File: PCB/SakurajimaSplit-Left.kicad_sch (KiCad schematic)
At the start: 31 parts, among them J1 SWD, J2 USB-C to Right-Half, J3 VREF+, SW1 SWCLK/BOOT0, U1 USBLC6-2SC6, U10 ZJY_M233, U2 STM32G0B1CBT6, U3 W25Q128JVS, Y1 8MHz

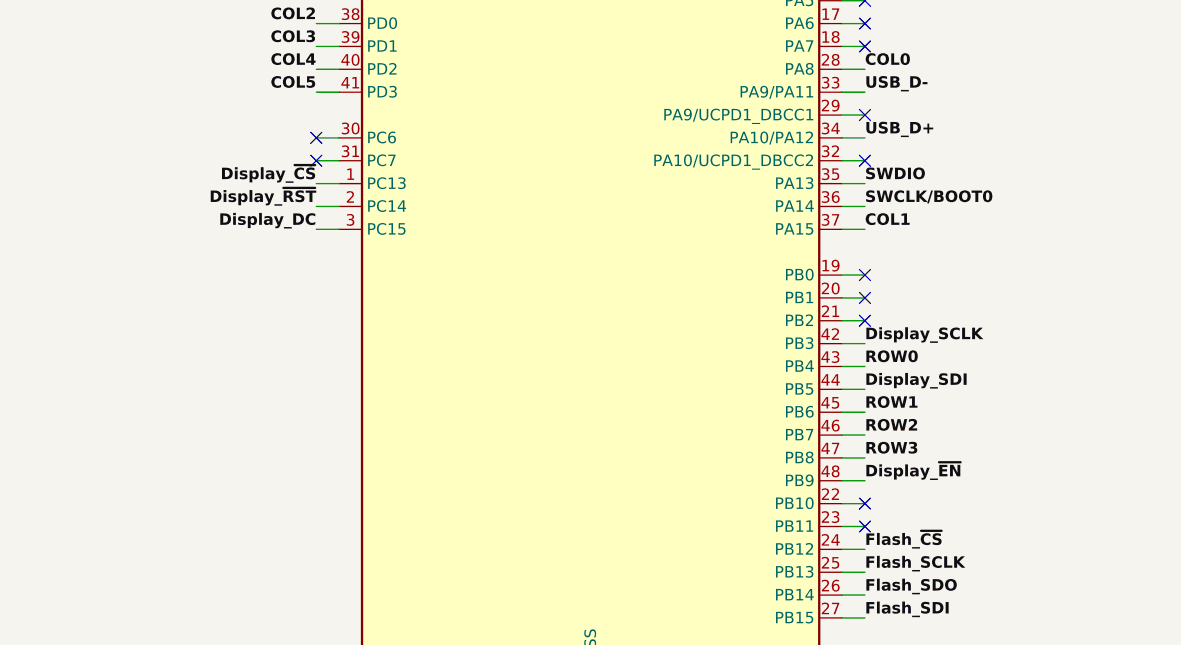
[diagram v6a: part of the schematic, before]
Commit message: feat(pcb): route left half
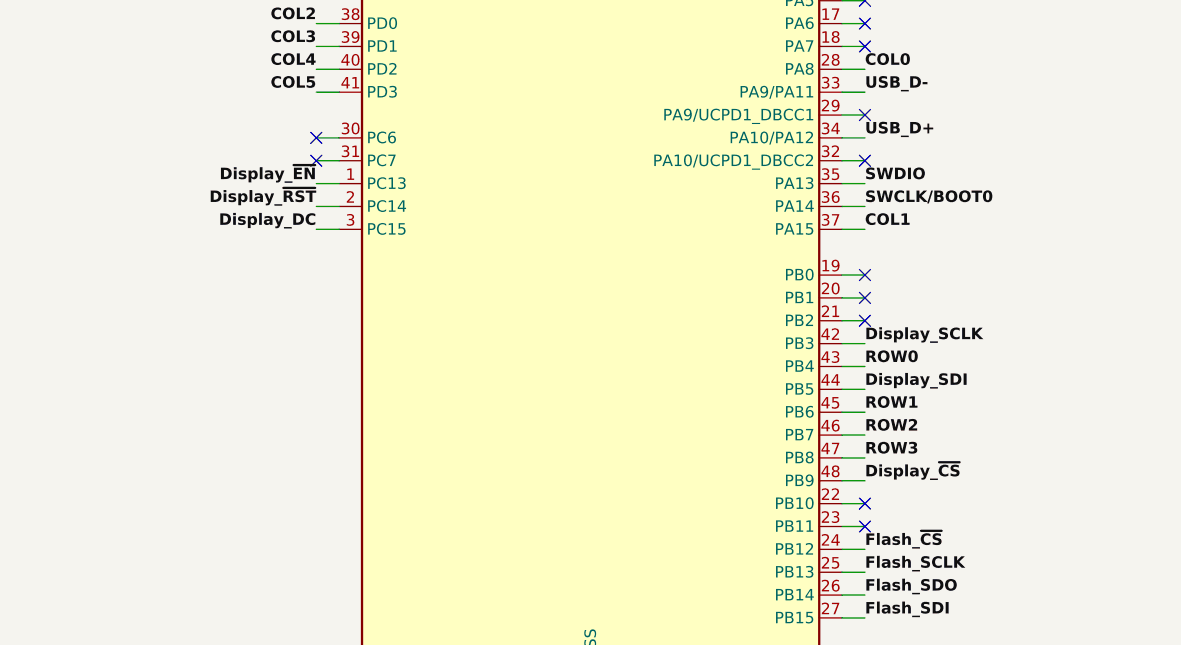
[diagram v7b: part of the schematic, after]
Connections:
- net Display_~{CS}: now also U2.48 (PB9); no longer U2.1 (PC13)
- net Display_~{EN}: now also U2.1 (PC13); no longer U2.48 (PB9)
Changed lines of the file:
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@@
 	)
 	(label "Display_~{CS}"
-		(at 179.07 147.32 180)
-		(effects
-			(font
-				(size 1.27 1.27)
-				(thickness 0.254)
-				(bold yes)
-			)
-			(justify right bottom)
+		(at 240.03 180.34 0)
+		(effects
+			(font
+				(size 1.27 1.27)
+				(thickness 0.254)
+				(bold yes)
+			)
+			(justify left bottom)
 		)
 	)
@@
 	)
 	(label "Display_~{EN}"
-		(at 240.03 180.34 0)
-		(effects
-			(font
-				(size 1.27 1.27)
-				(thickness 0.254)
-				(bold yes)
-			)
-			(justify left bottom)
-		)
-	)
+		(at 179.07 147.32 180)
+		(effects
+			(font
+				(size 1.27 1.27)
+				(thickness 0.254)
+				(bold yes)
+			)
+			(justify right bottom)
+		)
+	)

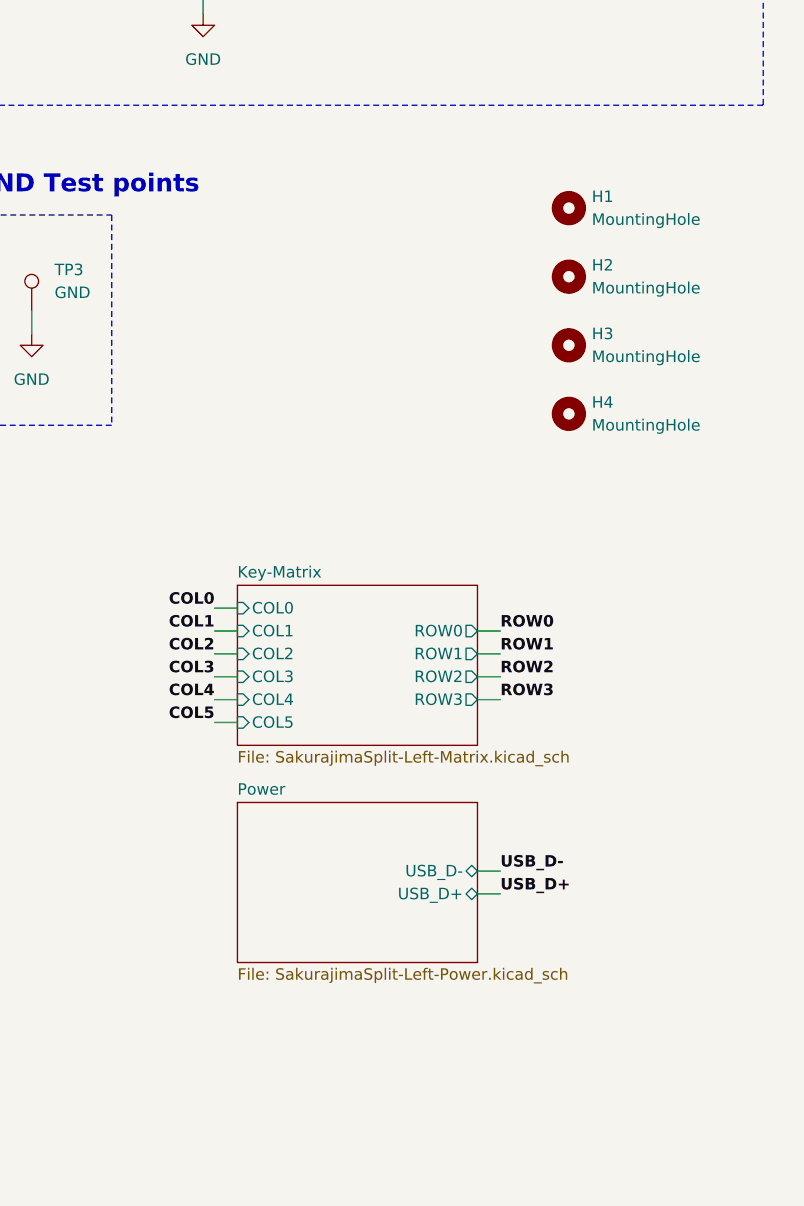
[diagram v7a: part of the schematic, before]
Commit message: feat(pcb): add mounting holes, fix some bugs
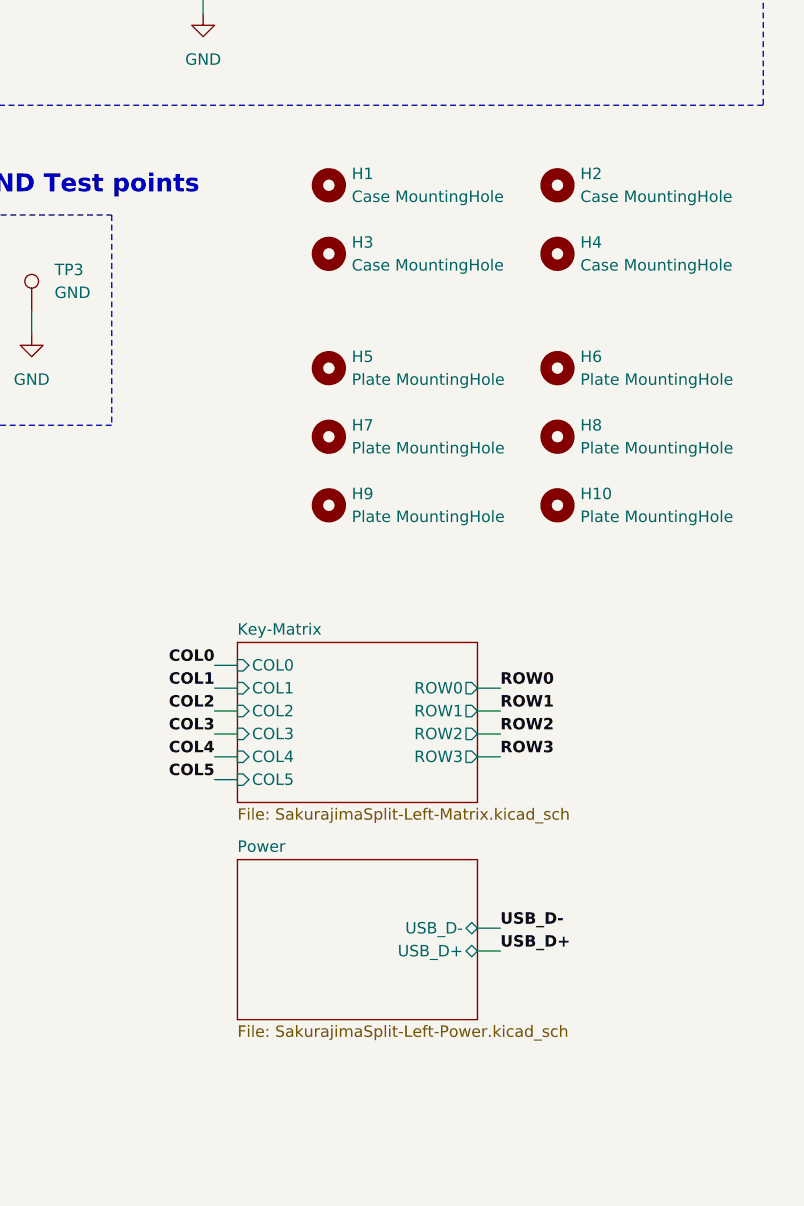
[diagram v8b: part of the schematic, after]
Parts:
- added H10, H5, H6, H7, H8, H9: Plate MountingHole, MountingHole:MountingHole_2.2mm_M2_Pad_Via, symbol Mechanical:MountingHole
- C5: Distributor Link (none) -> https://lionelectronic.ir/products/4734-GRM188R72A104KA35D; Manufacturer (none) -> Murata; Manufacturer Part No. (none) -> GRM188R72A104KA35D
- H1, H4: value MountingHole -> Case MountingHole
- H2: renamed from H3; value MountingHole -> Case MountingHole
- H3: renamed from H2; value MountingHole -> Case MountingHole
- SW1: Distributor Link https://lionelectronic.ir/products/5092-TS-1187A-B-A-B -> https://lionelectronic.ir/products/5480-TS-1010B-B-A; Manufacturer Part No. TS-1187A-B-A-B -> TS-1010B-B-A
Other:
- moved on the sheet: H1, H2, H3, H4
